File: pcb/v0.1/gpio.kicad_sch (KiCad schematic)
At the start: 33 parts, among them J5 Micro_SD_molex, J7 AudioJack3, SW1 SW_Push_45deg, U3 PCM5102A, U4 RT9742GGJ5, U7 RT9742GGJ5

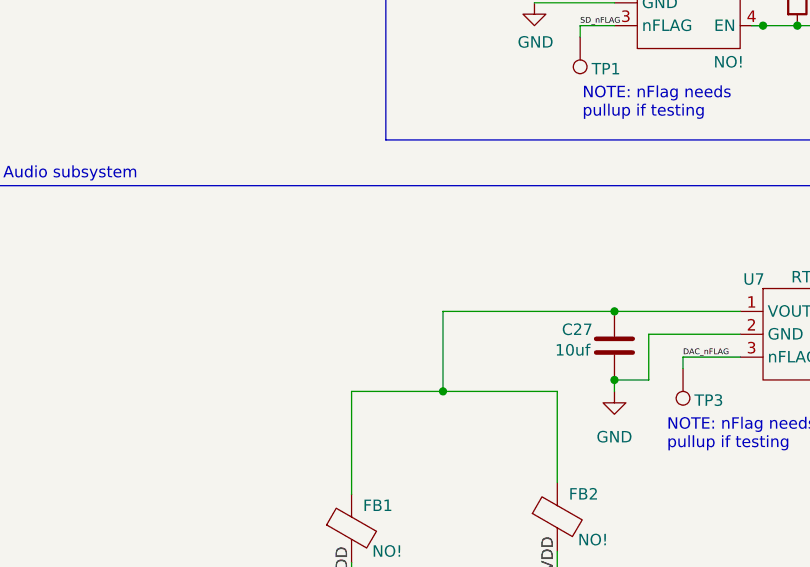
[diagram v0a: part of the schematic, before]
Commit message: Add bypass test point to power dac if switch is not working.
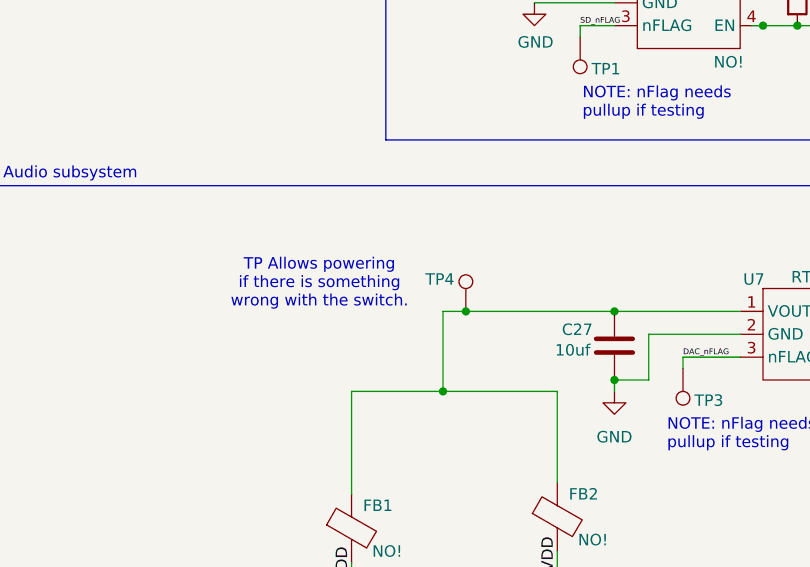
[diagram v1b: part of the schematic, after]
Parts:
- added TP4: TestPoint, symbol Connector:TestPoint
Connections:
- net at C27.2, FB1.1, FB2.1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: now also TP4.1
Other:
- note added: "TP Allows powering if there is something wrong with the switch."
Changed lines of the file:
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@@
 		)
 	)
+	(text "TP Allows powering\nif there is something\nwrong with the switch."
+		(exclude_from_sim no)
+		(at 320.294 140.462 0)
+		(effects
+			(font
+				(size 1.27 1.27)
+			)
+		)
+	)
 	(text "RPI boot SD card"
 		(exclude_from_sim no)
@@
 	)
 	(junction
+		(at 336.55 143.51)
+		(diameter 0)
+		(color 0 0 0 0)
+	)
+	(junction
 		(at 375.92 195.58)
 		(diameter 0)
@@
 	(wire
 		(pts
-			(xy 353.06 143.51) (xy 334.01 143.51)
+			(xy 353.06 143.51) (xy 336.55 143.51)
 		)
 		(stroke
@@
 	(wire
 		(pts
+			(xy 336.55 143.51) (xy 334.01 143.51)
+		)
+		(stroke
+			(width 0)
+			(type default)
+		)
+	)
+	(wire
+		(pts
 			(xy 317.5 203.2) (xy 322.58 203.2)
 		)
@@
 					(unit 1)
 				)
+			)
+		)
+	)
+	(symbol
+		(lib_id "Connector:TestPoint")
+		(at 336.55 143.51 0)
+		(unit 1)
+		(body_style 1)
+		(exclude_from_sim no)
+		(in_bom yes)
+		(on_board yes)
+		(in_pos_files yes)
+		(dnp no)
+		(property "Reference" "TP4"
+			(at 335.28 139.954 0)
+			(show_name no)
+			(do_not_autoplace no)
+			(effects
+				(font
+					(size 1.27 1.27)
+				)
+				(justify right)
+			)
+		)
+		(property "Value" "TestPoint"
+			(at 334.01 138.9381 0)
+			(hide yes)
+			(show_name no)
+			(do_not_autoplace no)
+			(effects
+				(font
+					(size 1.27 1.27)
+				)
+				(justify right)
+			)
+		)
+		(property "Footprint" ""
+			(at 341.63 143.51 0)
+			(hide yes)
+			(show_name no)
+			(do_not_autoplace no)
+			(effects
+				(font
+					(size 1.27 1.27)
+				)
+			)
+		)
+		(property "Datasheet" ""
+			(at 341.63 143.51 0)
+			(hide yes)
+			(show_name no)
+			(do_not_autoplace no)
+			(effects
+				(font
+					(size 1.27 1.27)
+				)
+			)
+		)
+		(property "Description" "test point"
+			(at 336.55 143.51 0)
+			(hide yes)
+			(show_name no)
+			(do_not_autoplace no)
+			(effects
+				(font
+					(size 1.27 1.27)
+				)
+			)
+		)
+		(pin "1"
+		)
+		(instances
+			(project "mainboard"
+				(path "/5b8aa782-5c3d-43e7-a869-3bd000015f52/5721f8f0-0440-46b6-aeef-45d87b753dcc"
+					(reference "TP4")
+					(unit 1)
+				)

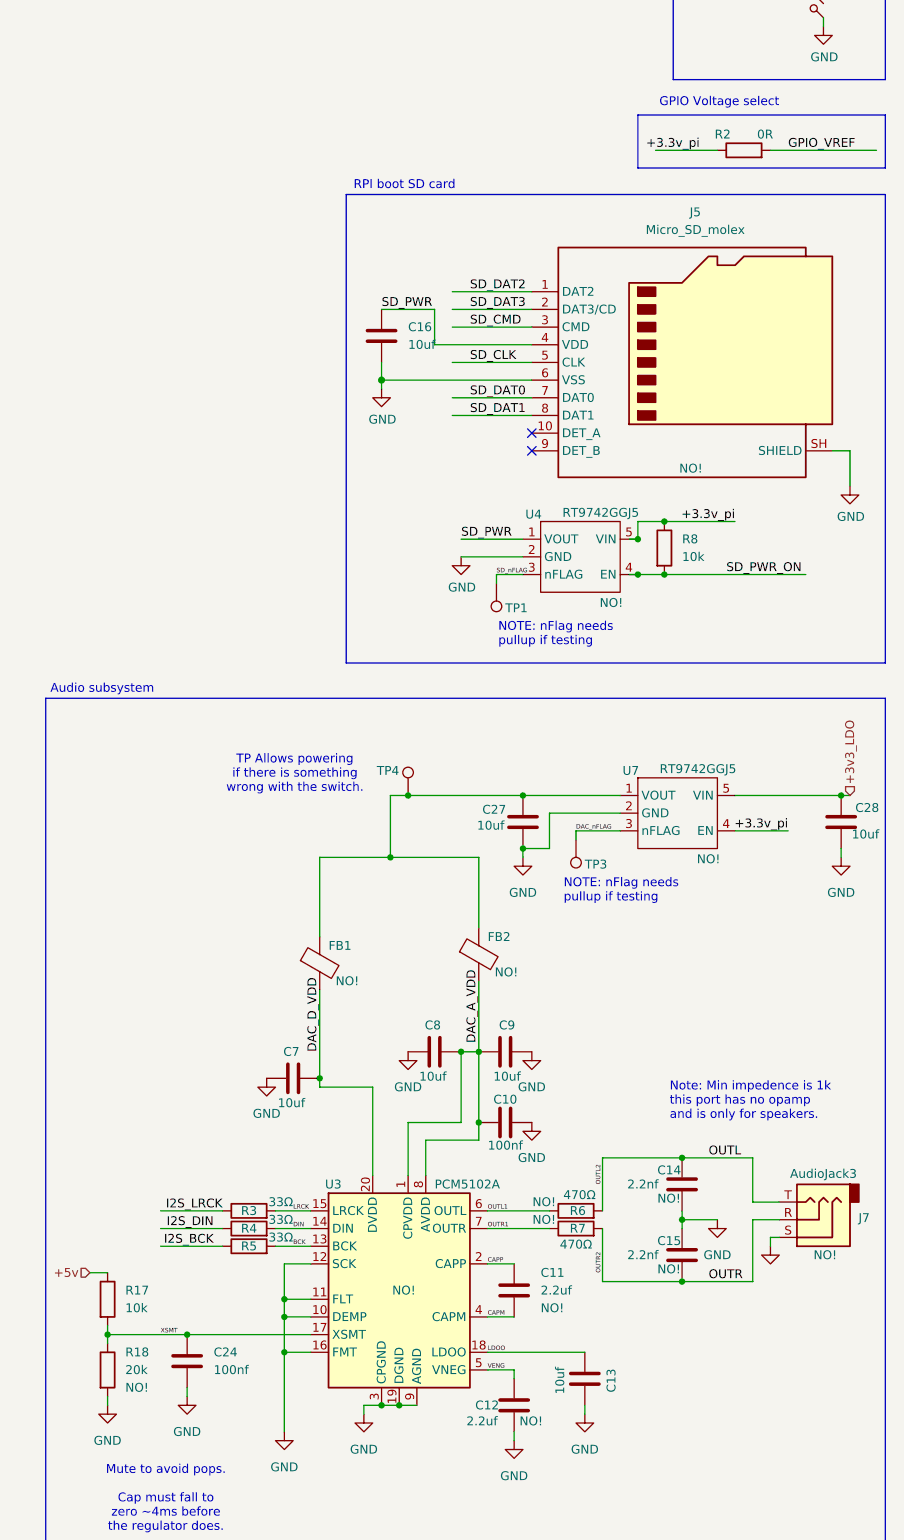
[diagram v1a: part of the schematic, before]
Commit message: Add pullup for nRESET of the nRF.
Also re-annotated all of the symbol numbers as they were starting to get
out of hand.
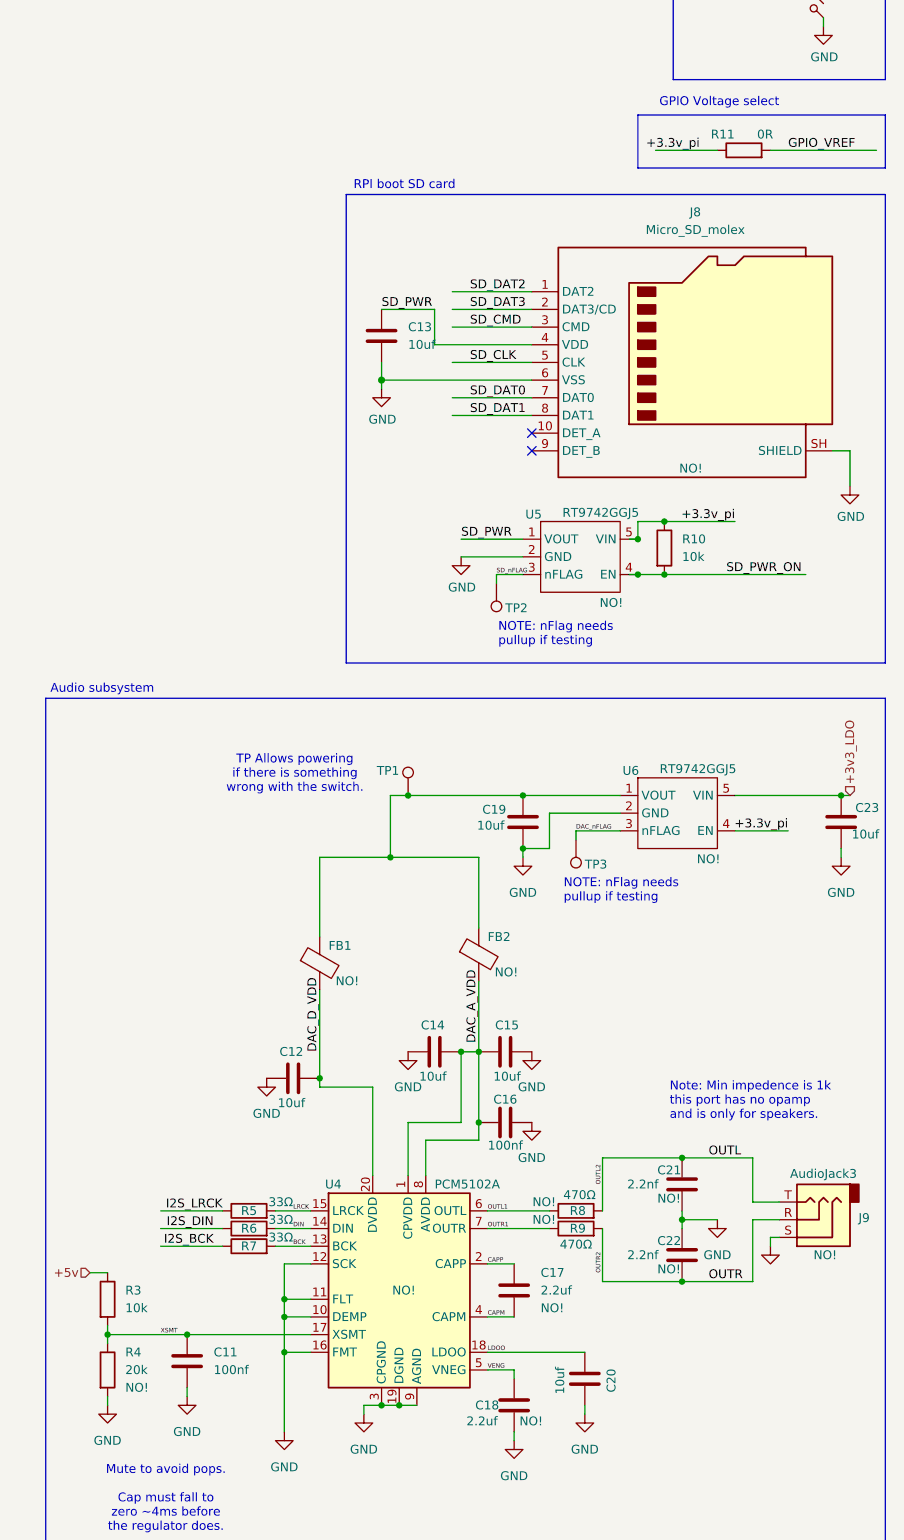
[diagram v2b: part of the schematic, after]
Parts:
- renumbered C24 to C11, C7 to C12, C16 to C13, C8 to C14, C9 to C15, C10 to C16, C11 to C17, C12 to C18, C27 to C19, C13 to C20, C14 to C21, C15 to C22, C28 to C23, J5 to J8, J7 to J9, R8 to R10, R2 to R11, R17 to R3, R18 to R4, R3 to R5, R4 to R6, R5 to R7, R6 to R8, R7 to R9, TP4 to TP1, TP1 to TP2, U3 to U4, U4 to U5, U7 to U6

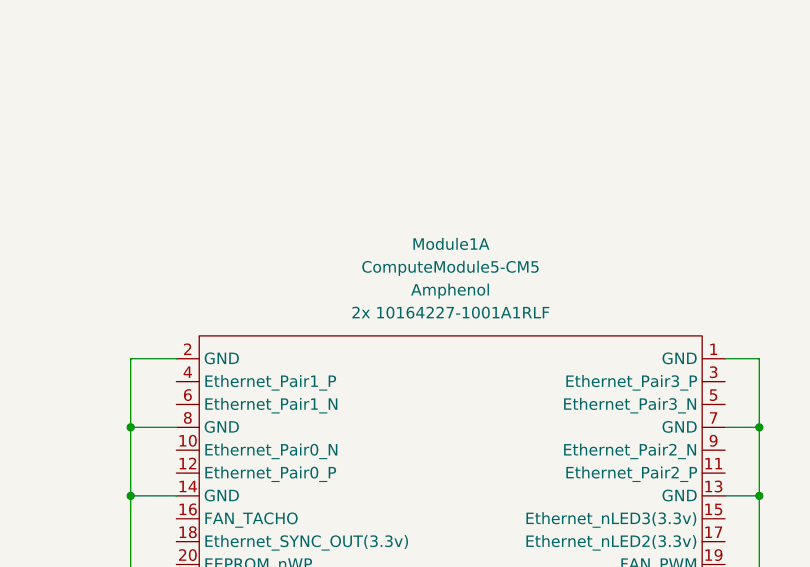
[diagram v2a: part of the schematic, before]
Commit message: Add connector for CM5
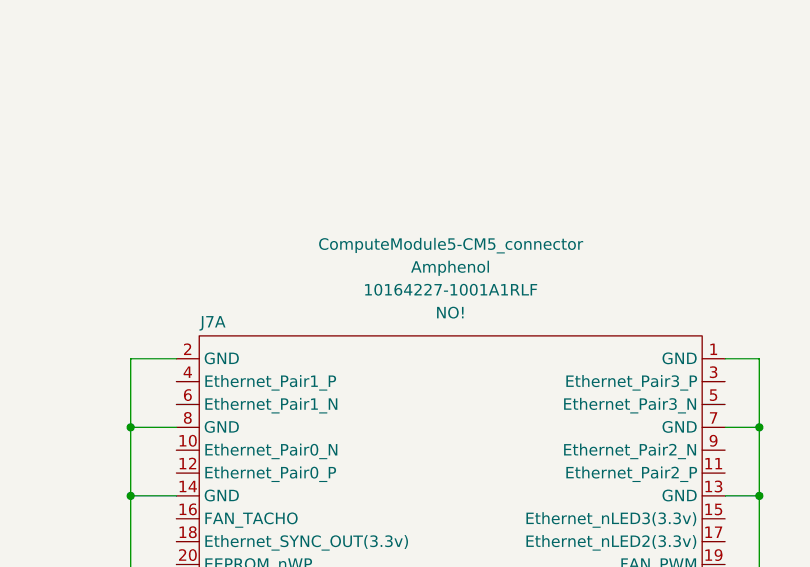
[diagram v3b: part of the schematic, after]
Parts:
- removed Module1: ComputeModule5-CM5, CM5IO:Raspberry-Pi-5-Compute-Module, symbol CM5IO:ComputeModule5-CM5
- added J7: ComputeModule5-CM5_connector, symbol TH-1-CC:ComputeModule5-CM5_connectors
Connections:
- net +3v3_PI: now also J7.84 (+3.3v_(Output)), J7.86 (+3.3v_(Output))
- net +5v: now also J7.77 (+5v_(Input)), J7.79 (+5v_(Input)), J7.81 (+5v_(Input)), J7.83 (+5v_(Input)), J7.85 (+5v_(Input)), J7.87 (+5v_(Input))
- net GND: now also J7.1 (GND), J7.13 (GND), J7.14 (GND), J7.2 (GND), J7.22 (GND), J7.23 (GND), J7.32 (GND), J7.33 (GND), J7.42 (GND), J7.43 (GND), J7.52 (GND), J7.53 (GND), J7.59 (GND), J7.60 (GND), J7.65 (GND), J7.66 (GND), J7.7 (GND), J7.71 (GND), J7.74 (GND), J7.8 (GND), J7.98 (GND)
- net GPIO_VREF: now also J7.78 (GPIO_VREF(1.8v/3.3v_Input))
- net I2S_BCK: now also J7.49 (GPIO18)
- net I2S_DIN: now also J7.25 (GPIO21)
- net I2S_LRCK: now also J7.26 (GPIO19)
- net MOD0: now also J7.37 (GPIO7)
- net MOD1: now also J7.39 (GPIO8)
- net MOD2: now also J7.41 (GPIO25)
- net MOD3: now also J7.45 (GPIO24)
- net PWR_BUT: now also J7.92 (PWR_BUT)
- net SCL3: now also J7.47 (GPIO23)
- net SDA3: now also J7.46 (GPIO22)
- net SD_CLK: now also J7.57 (SD_CLK)
- net SD_DAT0: now also J7.63 (SD_DAT0)
- net SD_DAT1: now also J7.67 (SD_DAT1)
- net SD_DAT2: now also J7.69 (SD_DAT2)
- net SD_DAT3: now also J7.61 (SD_DAT3)
- net SD_PWR_ON: now also J7.75 (SD_PWR_ON)
- net SWDCLK: now also J7.27 (GPIO20)
- net SWDIO: now also J7.30 (GPIO6)
- net U0_RX: now also J7.55 (GPIO14)
- net U0_TX: now also J7.51 (GPIO15)
- net U1_RX: now also J7.28 (GPIO13)
- net U1_TX: now also J7.31 (GPIO12)
- net USB2_CC1: now also J7.94 (CC1)
- net USB2_CC2: now also J7.96 (CC2)
- net nRESET: now also J7.29 (GPIO16)

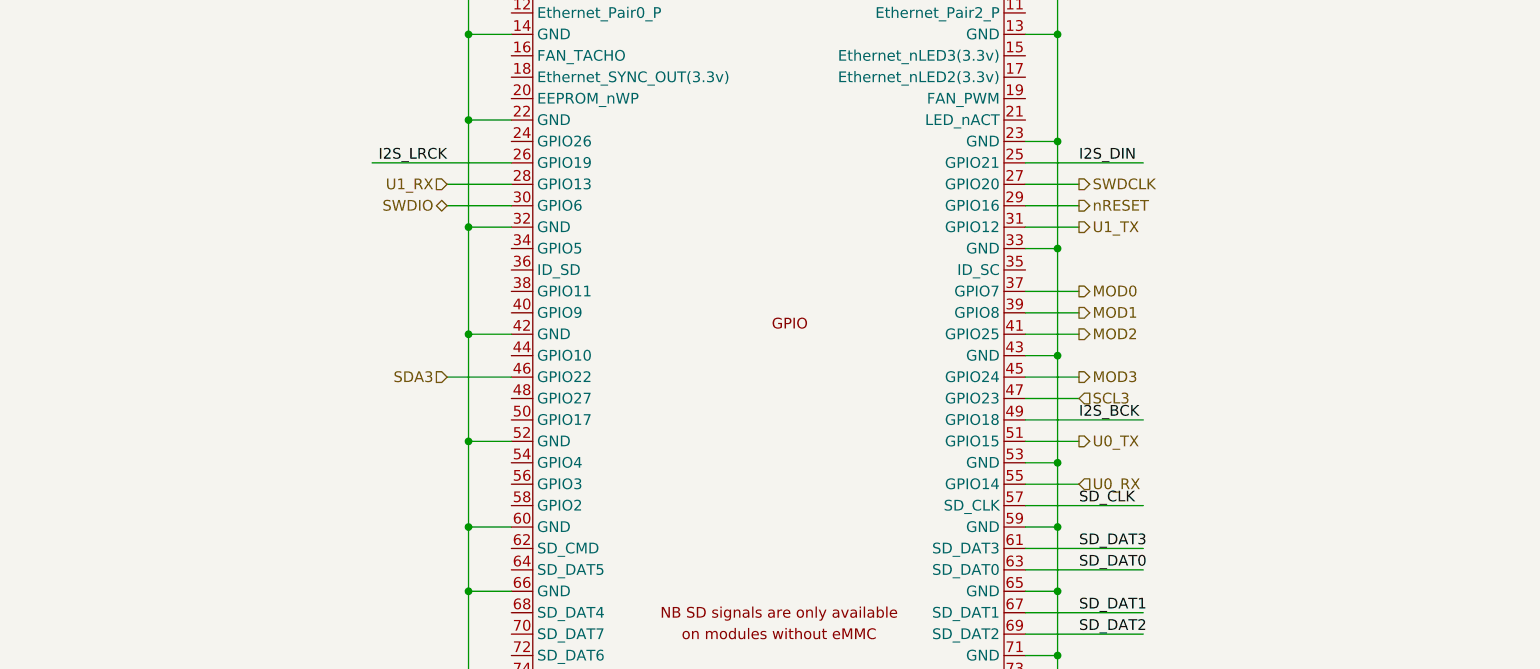
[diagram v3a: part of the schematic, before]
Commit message: Pinout for CM5 and co processor.
I've tried to make the pinout expose as many different protocols as
possible. Standard GPIO exists, but it was not a priority as I think its
more important to have protocols for the backpack.

The co processor also has 8 pins tied as input only. These are
technically I/O, but they have a resistor on them which may mess up some
output operations.
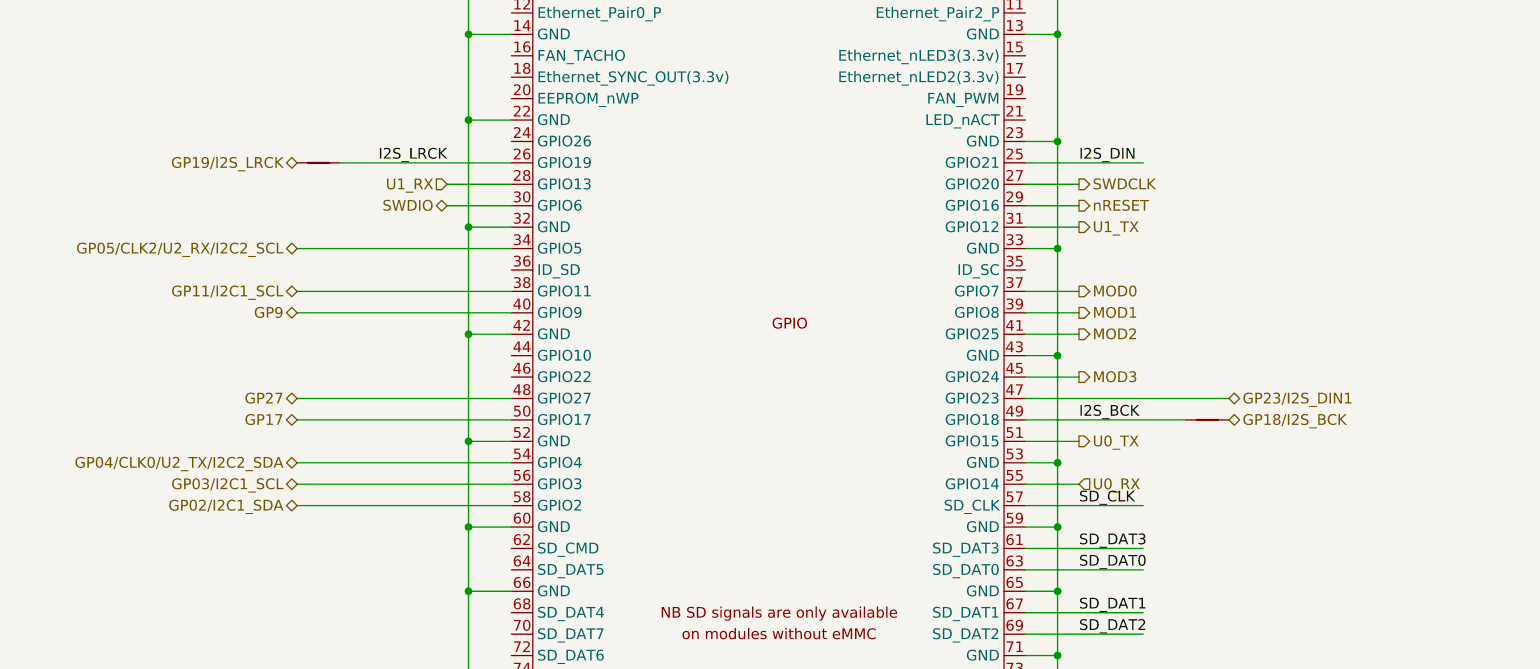
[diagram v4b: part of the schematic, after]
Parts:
- added NT1, NT2: NetTie_2, symbol Device:NetTie_2
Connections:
- net I2S_BCK: now also NT1.1
- net I2S_LRCK: now also NT2.1
- net GP05/CLK2/U2_RX/I2C2_SCL: now reaches J7.34 (GPIO5)
- net GP11/I2C1_SCL: now reaches J7.38 (GPIO11)
- net GP9: now reaches J7.40 (GPIO9)
- net GP27: now reaches J7.48 (GPIO27)
- net GP17: now reaches J7.50 (GPIO17)
- net GP04/CLK0/U2_TX/I2C2_SDA: now reaches J7.54 (GPIO4)
- net GP03/I2C1_SCL: now reaches J7.56 (GPIO3)
- net GP02/I2C1_SDA: now reaches J7.58 (GPIO2)
- net SCL3 renamed GP23/I2S_DIN1
- net SDA3: no longer names the net of J7.46 (GPIO22)
- new net GP18/I2S_BCK: NT1.2
- new net GP19/I2S_LRCK: NT2.2
